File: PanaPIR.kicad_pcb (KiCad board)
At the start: 2 copper layers, 23 x 23 mm, 5 parts, among them P1 HEADER, P2 HEADER, U1 PIR

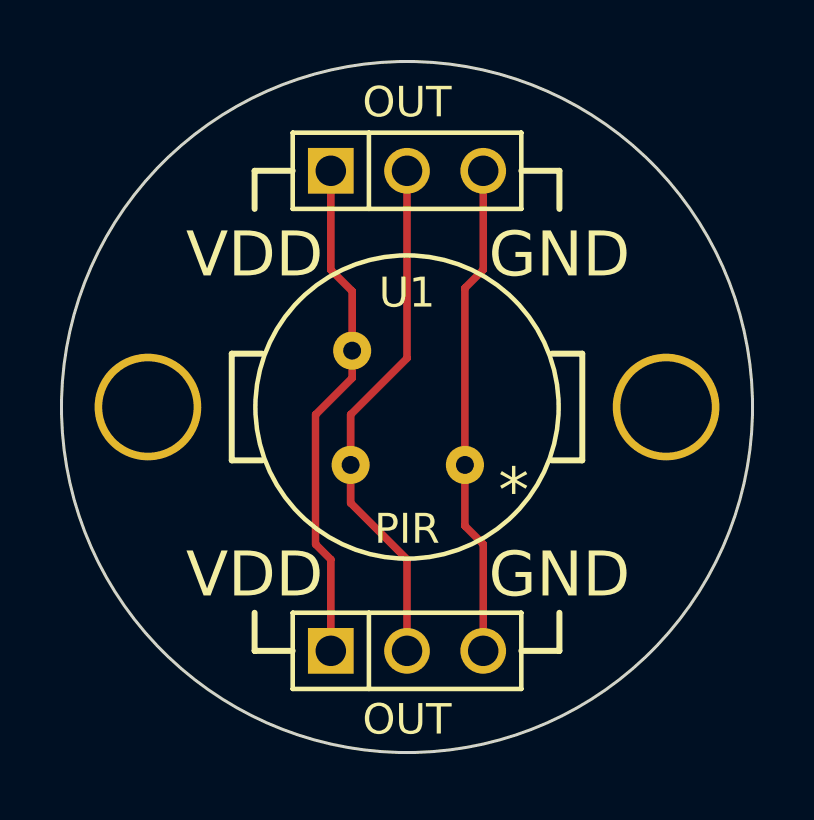
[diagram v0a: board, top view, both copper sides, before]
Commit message: Make PCB more compatible with breadboards
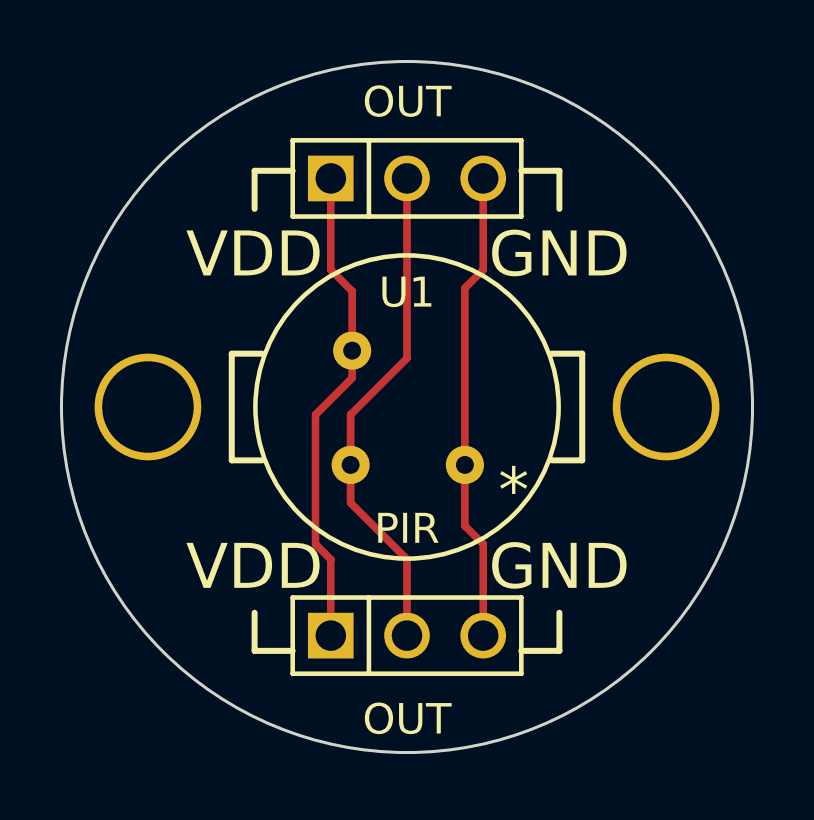
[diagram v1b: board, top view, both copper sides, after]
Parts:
- moved P1 0.51 mm to (209.0, 155.7)
- moved P2 0.25 mm to (209.0, 140.5)
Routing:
- net N-000003: track 17.0 -> 16.3 mm
- net N-000002: track 17.6 -> 16.8 mm
- net N-000001: track 16.5 -> 15.7 mm
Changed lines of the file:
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@@
   )
   (module PIN_ARRAY_3X1 (layer F.Cu)
-    (at 209.042 140.208)
+    (at 209.042 140.462)
     (descr "Connecteur 3 pins")
     (tags "CONN DEV")
@@
   )
   (module PIN_ARRAY_3X1 (layer F.Cu)
-    (at 209.042 156.21)
+    (at 209.042 155.702)
     (descr "Connecteur 3 pins")
     (tags "CONN DEV")
@@
     (effects (font (size 1.5 1.5) (thickness 0.3)))
   )
-  (gr_text VDD (at 203.962 153.67) (layer F.SilkS)
+  (gr_text VDD (at 203.962 153.416) (layer F.SilkS)
     (effects (font (size 1.5 1.5) (thickness 0.3)))
   )
-  (gr_text GND (at 214.122 153.67) (layer F.SilkS)
+  (gr_text GND (at 214.122 153.416) (layer F.SilkS)
     (effects (font (size 1.5 1.5) (thickness 0.3)))
   )
@@
     (effects (font (size 1.5 1.5) (thickness 0.3)) (justify mirror))
   )
-  (gr_text VDD (at 203.962 153.67) (layer B.SilkS)
+  (gr_text VDD (at 203.962 153.416) (layer B.SilkS)
     (effects (font (size 1.5 1.5) (thickness 0.3)) (justify mirror))
   )
-  (gr_text OUT (at 209.042 153.67) (layer B.SilkS)
+  (gr_text OUT (at 209.042 153.416) (layer B.SilkS)
     (effects (font (size 1.5 1.5) (thickness 0.3)) (justify mirror))
   )
-  (gr_text GND (at 214.122 153.67) (layer B.SilkS)
+  (gr_text GND (at 214.122 153.416) (layer B.SilkS)
     (effects (font (size 1.5 1.5) (thickness 0.3)) (justify mirror))
   )
@@
   )
   (segment (start 210.9724 150.0124) (end 210.9724 144.1196) (width 0.254) (layer F.Cu) (net 1) (status 10))
-  (segment (start 211.582 143.51) (end 211.582 140.208) (width 0.254) (layer F.Cu) (net 1) (status 20))
+  (segment (start 211.582 143.51) (end 211.582 140.462) (width 0.254) (layer F.Cu) (net 1) (status 800020))
   (segment (start 210.9724 144.1196) (end 211.582 143.51) (width 0.254) (layer F.Cu) (net 1))
   (segment (start 210.9724 150.0124) (end 210.9724 152.0444) (width 0.254) (layer F.Cu) (net 1) (status 10))
-  (segment (start 211.582 152.654) (end 211.582 156.21) (width 0.254) (layer F.Cu) (net 1) (status 20))
+  (segment (start 211.582 152.654) (end 211.582 155.702) (width 0.254) (layer F.Cu) (net 1) (status 800020))
   (segment (start 210.9724 152.0444) (end 211.582 152.654) (width 0.254) (layer F.Cu) (net 1))
-  (segment (start 207.1624 150.0124) (end 207.1624 148.336) (width 0.254) (layer F.Cu) (net 2) (status 400000))
-  (segment (start 209.042 146.4564) (end 209.042 140.208) (width 0.254) (layer F.Cu) (net 2) (status 800000))
+  (segment (start 207.1624 150.0124) (end 207.1624 148.336) (width 0.254) (layer F.Cu) (net 2))
+  (segment (start 209.042 146.4564) (end 209.042 140.462) (width 0.254) (layer F.Cu) (net 2) (status 800000))
   (segment (start 207.1624 148.336) (end 209.042 146.4564) (width 0.254) (layer F.Cu) (net 2))
   (segment (start 207.1624 150.0124) (end 207.1624 151.2824) (width 0.254) (layer F.Cu) (net 2) (status 10))
-  (segment (start 209.042 153.162) (end 209.042 156.21) (width 0.254) (layer F.Cu) (net 2) (status 20))
+  (segment (start 209.042 153.162) (end 209.042 155.702) (width 0.254) (layer F.Cu) (net 2) (status 800020))
   (segment (start 207.1624 151.2824) (end 209.042 153.162) (width 0.254) (layer F.Cu) (net 2))
   (segment (start 207.2132 146.2024) (end 207.2132 147.1168) (width 0.254) (layer F.Cu) (net 3) (status 10))
-  (segment (start 206.502 153.162) (end 206.502 156.21) (width 0.254) (layer F.Cu) (net 3) (status 20))
+  (segment (start 206.502 153.162) (end 206.502 155.702) (width 0.254) (layer F.Cu) (net 3) (status 800020))
   (segment (start 205.994 152.654) (end 206.502 153.162) (width 0.254) (layer F.Cu) (net 3))
   (segment (start 205.994 148.336) (end 205.994 152.654) (width 0.254) (layer F.Cu) (net 3))
   (segment (start 207.2132 147.1168) (end 205.994 148.336) (width 0.254) (layer F.Cu) (net 3))
   (segment (start 207.2132 146.2024) (end 207.2132 144.2212) (width 0.254) (layer F.Cu) (net 3) (status 10))
-  (segment (start 206.502 143.51) (end 206.502 140.208) (width 0.254) (layer F.Cu) (net 3) (status 20))
+  (segment (start 206.502 143.51) (end 206.502 140.462) (width 0.254) (layer F.Cu) (net 3) (status 800020))
   (segment (start 207.2132 144.2212) (end 206.502 143.51) (width 0.254) (layer F.Cu) (net 3))
 )

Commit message: Add 0603 decoupling cap and better spacing for breadboards
600 mil center drill distance from top to bottom for PTH headers.
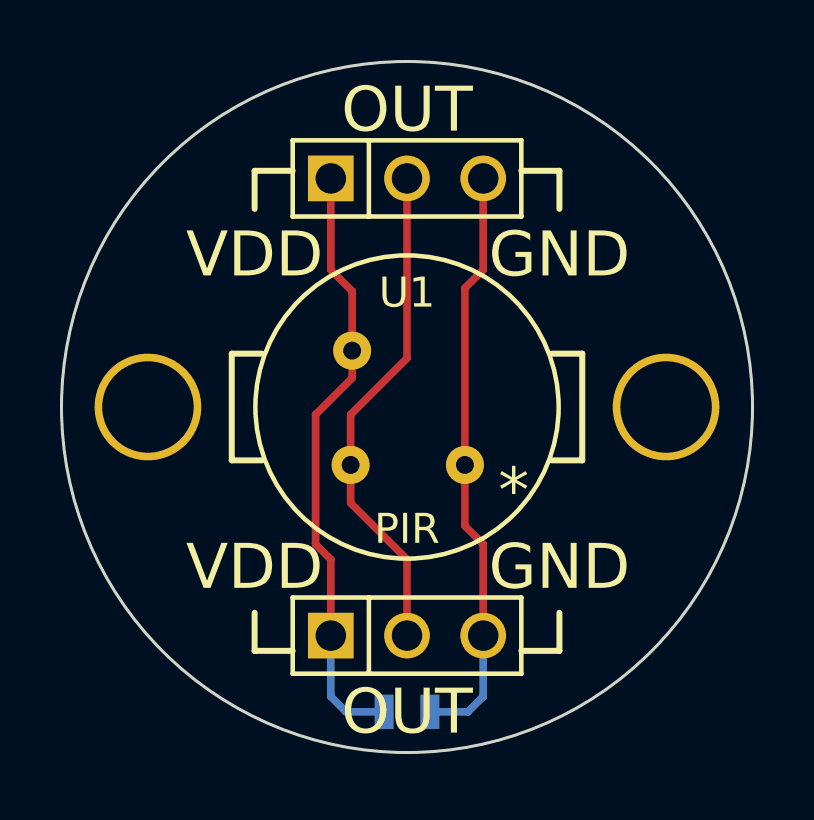
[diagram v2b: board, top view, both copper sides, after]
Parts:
- added C1: 0.1uF, SM0603_Capa, B.Cu at (209.0, 158.2)
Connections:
- net N-000001 renamed GND
- net N-000003 renamed +3.3V
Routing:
- net GND: track 15.7 -> 19.8 mm
- net +3.3V: track 16.3 -> 20.3 mm
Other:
- board text added: "2014-04-08"
- board text removed: "adcb49f"
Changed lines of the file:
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@@
 (kicad_pcb (version 3) (host pcbnew "(2013-june-11)-stable")
   (general
-    (links 6)
+    (links 8)
     (no_connects 0)
     (area 197.474842 136.514842 220.609158 159.649158)
     (thickness 1.6)
-    (drawings 39)
-    (tracks 20)
+    (drawings 40)
+    (tracks 26)
     (zones 0)
-    (modules 5)
+    (modules 6)
     (nets 4)
   )
@@
   )
   (net 0 "")
-  (net 1 N-000001)
-  (net 2 N-000002)
-  (net 3 N-000003)
+  (net 1 +3.3V)
+  (net 2 GND)
+  (net 3 N-000002)
   (net_class Default "This is the default net class."
     (clearance 0.254)
@@
     (uvia_drill 0.127)
     (add_net "")
-    (add_net N-000001)
+    (add_net +3.3V)
+    (add_net GND)
     (add_net N-000002)
-    (add_net N-000003)
   )
   (module PIR (layer F.Cu)
@@
     (pad 1 thru_hole circle (at -1.8288 -1.8796 180) (size 1.27 1.27) (drill 0.5969)
       (layers *.Cu *.Mask F.SilkS)
-      (net 3 N-000003)
+      (net 1 +3.3V)
     )
     (pad 2 thru_hole circle (at -1.8796 1.9304 180) (size 1.27 1.27) (drill 0.5969)
       (layers *.Cu *.Mask F.SilkS)
-      (net 2 N-000002)
+      (net 3 N-000002)
     )
     (pad 3 thru_hole circle (at 1.9304 1.9304 180) (size 1.27 1.27) (drill 0.5969)
       (layers *.Cu *.Mask F.SilkS)
-      (net 1 N-000001)
+      (net 2 GND)
     )
   )
@@
     (pad 1 thru_hole rect (at -2.54 0) (size 1.524 1.524) (drill 1.016)
       (layers *.Cu *.Mask F.SilkS)
-      (net 3 N-000003)
+      (net 1 +3.3V)
     )
     (pad 2 thru_hole circle (at 0 0) (size 1.524 1.524) (drill 1.016)
       (layers *.Cu *.Mask F.SilkS)
-      (net 2 N-000002)
+      (net 3 N-000002)
     )
     (pad 3 thru_hole circle (at 2.54 0) (size 1.524 1.524) (drill 1.016)
       (layers *.Cu *.Mask F.SilkS)
-      (net 1 N-000001)
+      (net 2 GND)
     )
     (model pin_array/pins_array_3x1.wrl
@@
     (pad 1 thru_hole rect (at -2.54 0) (size 1.524 1.524) (drill 1.016)
       (layers *.Cu *.Mask F.SilkS)
-      (net 3 N-000003)
+      (net 1 +3.3V)
     )
     (pad 2 thru_hole circle (at 0 0) (size 1.524 1.524) (drill 1.016)
       (layers *.Cu *.Mask F.SilkS)
-      (net 2 N-000002)
+      (net 3 N-000002)
     )
     (pad 3 thru_hole circle (at 2.54 0) (size 1.524 1.524) (drill 1.016)
       (layers *.Cu *.Mask F.SilkS)
-      (net 1 N-000001)
+      (net 2 GND)
     )
     (model pin_array/pins_array_3x1.wrl
@@
       (layers *.Cu *.Mask F.SilkS)
     )
+  )
+  (module SM0603_Capa (layer B.Cu)
+    (at 209.042 158.242 180)
+    (attr smd)
+    (fp_text reference C1 (at 2.032 0 270) (layer B.SilkS)
+      (effects (font (size 1 1) (thickness 0.15)) (justify mirror))
+    )
+    (fp_text value 0.1uF (at -1.778 0 270) (layer B.SilkS) hide
+      (effects (font (size 0.508 0.4572) (thickness 0.1143)) (justify mirror))
+    )
+    (fp_line (start 0.50038 -0.65024) (end 1.19888 -0.65024) (layer B.SilkS) (width 0.11938))
+    (fp_line (start -0.50038 -0.65024) (end -1.19888 -0.65024) (layer B.SilkS) (width 0.11938))
+    (fp_line (start 0.50038 0.65024) (end 1.19888 0.65024) (layer B.SilkS) (width 0.11938))
+    (fp_line (start -1.19888 0.65024) (end -0.50038 0.65024) (layer B.SilkS) (width 0.11938))
+    (fp_line (start 1.19888 0.635) (end 1.19888 -0.635) (layer B.SilkS) (width 0.11938))
+    (fp_line (start -1.19888 -0.635) (end -1.19888 0.635) (layer B.SilkS) (width 0.11938))
+    (pad 1 smd rect (at -0.762 0 180) (size 0.635 1.143)
+      (layers B.Cu B.Paste B.Mask)
+      (net 2 GND)
+    )
+    (pad 2 smd rect (at 0.762 0 180) (size 0.635 1.143)
+      (layers B.Cu B.Paste B.Mask)
+      (net 1 +3.3V)
+    )
+    (model smd\capacitors\C0603.wrl
+      (at (xyz 0 0 0.001))
+      (scale (xyz 0.5 0.5 0.5))
+      (rotate (xyz 0 0 0))
+    )
+  )
+  (gr_text * (at 211.582 158.75) (layer B.SilkS)
+    (effects (font (size 1.5 1.5) (thickness 0.3)) (justify mirror))
   )
   (gr_line (start 214.122 156.21) (end 214.122 154.94) (angle 90) (layer F.SilkS) (width 0.2))
@@
   (gr_line (start 203.962 140.208) (end 203.962 141.478) (angle 90) (layer F.SilkS) (width 0.2))
   (gr_line (start 205.232 140.208) (end 203.962 140.208) (angle 90) (layer F.SilkS) (width 0.2))
-  (gr_text OUT (at 209.042 137.922) (layer F.SilkS)
-    (effects (font (size 1.016 1.016) (thickness 0.254)))
-  )
-  (gr_text OUT (at 209.042 158.496) (layer F.SilkS)
-    (effects (font (size 1.016 1.016) (thickness 0.254)))
+  (gr_text OUT (at 209.042 138.176) (layer F.SilkS)
+    (effects (font (size 1.5 1.5) (thickness 0.254)))
+  )
+  (gr_text OUT (at 209.042 158.242) (layer F.SilkS)
+    (effects (font (size 1.5 1.5) (thickness 0.254)))
   )
   (gr_text GND (at 214.122 143.002) (layer F.SilkS)
@@
     (effects (font (size 1.016 1.016) (thickness 0.254)) (justify mirror))
   )
-  (gr_text adcb49f (at 209.042 148.082) (layer B.Mask)
+  (gr_text 2014-04-08 (at 209.042 148.082) (layer B.Mask)
     (effects (font (size 1.016 1.016) (thickness 0.254)) (justify mirror))
   )
@@
     (effects (font (size 1.5 1.5) (thickness 0.3)))
   )
-  (segment (start 210.9724 150.0124) (end 210.9724 144.1196) (width 0.254) (layer F.Cu) (net 1) (status 10))
-  (segment (start 211.582 143.51) (end 211.582 140.462) (width 0.254) (layer F.Cu) (net 1) (status 800020))
-  (segment (start 210.9724 144.1196) (end 211.582 143.51) (width 0.254) (layer F.Cu) (net 1))
-  (segment (start 210.9724 150.0124) (end 210.9724 152.0444) (width 0.254) (layer F.Cu) (net 1) (status 10))
-  (segment (start 211.582 152.654) (end 211.582 155.702) (width 0.254) (layer F.Cu) (net 1) (status 800020))
-  (segment (start 210.9724 152.0444) (end 211.582 152.654) (width 0.254) (layer F.Cu) (net 1))
-  (segment (start 207.1624 150.0124) (end 207.1624 148.336) (width 0.254) (layer F.Cu) (net 2))
-  (segment (start 209.042 146.4564) (end 209.042 140.462) (width 0.254) (layer F.Cu) (net 2) (status 800000))
-  (segment (start 207.1624 148.336) (end 209.042 146.4564) (width 0.254) (layer F.Cu) (net 2))
-  (segment (start 207.1624 150.0124) (end 207.1624 151.2824) (width 0.254) (layer F.Cu) (net 2) (status 10))
-  (segment (start 209.042 153.162) (end 209.042 155.702) (width 0.254) (layer F.Cu) (net 2) (status 800020))
-  (segment (start 207.1624 151.2824) (end 209.042 153.162) (width 0.254) (layer F.Cu) (net 2))
-  (segment (start 207.2132 146.2024) (end 207.2132 147.1168) (width 0.254) (layer F.Cu) (net 3) (status 10))
-  (segment (start 206.502 153.162) (end 206.502 155.702) (width 0.254) (layer F.Cu) (net 3) (status 800020))
-  (segment (start 205.994 152.654) (end 206.502 153.162) (width 0.254) (layer F.Cu) (net 3))
-  (segment (start 205.994 148.336) (end 205.994 152.654) (width 0.254) (layer F.Cu) (net 3))
-  (segment (start 207.2132 147.1168) (end 205.994 148.336) (width 0.254) (layer F.Cu) (net 3))
-  (segment (start 207.2132 146.2024) (end 207.2132 144.2212) (width 0.254) (layer F.Cu) (net 3) (status 10))
-  (segment (start 206.502 143.51) (end 206.502 140.462) (width 0.254) (layer F.Cu) (net 3) (status 800020))
-  (segment (start 207.2132 144.2212) (end 206.502 143.51) (width 0.254) (layer F.Cu) (net 3))
+  (segment (start 206.502 155.702) (end 206.502 157.734) (width 0.254) (layer B.Cu) (net 1))
+  (segment (start 207.01 158.242) (end 208.28 158.242) (width 0.254) (layer B.Cu) (net 1))
+  (segment (start 206.502 157.734) (end 207.01 158.242) (width 0.254) (layer B.Cu) (net 1))
+  (segment (start 207.2132 146.2024) (end 207.2132 147.1168) (width 0.254) (layer F.Cu) (net 1) (status 10))
+  (segment (start 206.502 153.162) (end 206.502 155.702) (width 0.254) (layer F.Cu) (net 1) (status 20))
+  (segment (start 205.994 152.654) (end 206.502 153.162) (width 0.254) (layer F.Cu) (net 1))
+  (segment (start 205.994 148.336) (end 205.994 152.654) (width 0.254) (layer F.Cu) (net 1))
+  (segment (start 207.2132 147.1168) (end 205.994 148.336) (width 0.254) (layer F.Cu) (net 1))
+  (segment (start 207.2132 146.2024) (end 207.2132 144.2212) (width 0.254) (layer F.Cu) (net 1) (status 10))
+  (segment (start 206.502 143.51) (end 206.502 140.462) (width 0.254) (layer F.Cu) (net 1) (status 20))
+  (segment (start 207.2132 144.2212) (end 206.502 143.51) (width 0.254) (layer F.Cu) (net 1))
+  (segment (start 211.582 155.702) (end 211.582 157.734) (width 0.254) (layer B.Cu) (net 2))
+  (segment (start 211.074 158.242) (end 209.804 158.242) (width 0.254) (layer B.Cu) (net 2))
+  (segment (start 211.582 157.734) (end 211.074 158.242) (width 0.254) (layer B.Cu) (net 2))
+  (segment (start 210.9724 150.0124) (end 210.9724 144.1196) (width 0.254) (layer F.Cu) (net 2) (status 10))
+  (segment (start 211.582 143.51) (end 211.582 140.462) (width 0.254) (layer F.Cu) (net 2) (status 20))
+  (segment (start 210.9724 144.1196) (end 211.582 143.51) (width 0.254) (layer F.Cu) (net 2))
+  (segment (start 210.9724 150.0124) (end 210.9724 152.0444) (width 0.254) (layer F.Cu) (net 2) (status 10))
+  (segment (start 211.582 152.654) (end 211.582 155.702) (width 0.254) (layer F.Cu) (net 2) (status 20))
+  (segment (start 210.9724 152.0444) (end 211.582 152.654) (width 0.254) (layer F.Cu) (net 2))
+  (segment (start 207.1624 150.0124) (end 207.1624 148.336) (width 0.254) (layer F.Cu) (net 3))
+  (segment (start 209.042 146.4564) (end 209.042 140.462) (width 0.254) (layer F.Cu) (net 3))
+  (segment (start 207.1624 148.336) (end 209.042 146.4564) (width 0.254) (layer F.Cu) (net 3))
+  (segment (start 207.1624 150.0124) (end 207.1624 151.2824) (width 0.254) (layer F.Cu) (net 3) (status 10))
+  (segment (start 209.042 153.162) (end 209.042 155.702) (width 0.254) (layer F.Cu) (net 3) (status 20))
+  (segment (start 207.1624 151.2824) (end 209.042 153.162) (width 0.254) (layer F.Cu) (net 3))
 )
